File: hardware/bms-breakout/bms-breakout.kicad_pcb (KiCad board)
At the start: 2 copper layers, 115.6 x 85.8 mm, 14 parts, among them J1 IN-A, J10 V-SUPP, J11 Smol_Brain_Board, J12 DE9_Socket_MountingHoles, J13 UART_CONN, J15 SBB_POWER, J2 IN-B, J3 IN-C, J4 BALANCE-A, J5 BALANCE-B, J6 BALANCE-C, J8 BMS-OUT, J9 BMS-IN

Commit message: WIP: Starting firmware and routing pcb
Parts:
- moved J15 79.1 mm to (148.2, 124.0), turned to 180 degrees
- moved J9 10.1 mm to (174.9, 112.6)
- moved J10 9.91 mm to (155.3, 91.5)
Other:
- board size 115.6 x 85.8 mm -> 125.8 x 85.8 mm
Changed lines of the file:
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@@
 	(version 20241229)
 	(generator "pcbnew")
-	(generator_version "9.0")
+	(generator_version "9.99")
 	(general
 		(thickness 1.6)
@@
 	(footprint "Connector_AMASS:AMASS_XT90PW-M_1x02_P10.90mm_Horizontal"
 		(layer "F.Cu")
-		(at 164.85 112.05 180)
+		(at 174.9 112.6 180)
 		(descr "Connector XT90 Horizontal PCB Male  500V 30A IP40, https://www.bto.pl/pdf/09025/XT90PW-M.pdf")
 		(tags "RC")
@@
 	(footprint "Connector_AMASS:AMASS_XT30PW-M_1x02_P2.50mm_Horizontal"
 		(layer "F.Cu")
-		(at 69.575 115.2 90)
+		(at 148.2 124 180)
 		(descr "Connector XT30 Horizontal PCB Male, https://www.tme.eu/Document/6eb2005a51a52592b3f19e8a450c54c8/XT30PW-M.pdf")
 		(tags "RC Connector XT30")
 		(property "Reference" "J15"
-			(at 2.4 -2.675 90)
+			(at 2.4 -2.675 0)
 			(layer "F.SilkS")
 			(effects
@@
 		)
 		(property "Value" "SBB_POWER"
-			(at -2.5 3.5 90)
+			(at -2.5 3.5 0)
 			(layer "F.Fab")
 			(effects
@@
 		)
 		(property "Datasheet" "~"
-			(at 0 0 90)
+			(at 0 0 180)
 			(unlocked yes)
 			(layer "F.Fab")
@@
 		)
 		(property "Description" "Generic connectable mounting pin connector, single row, 01x02, script generated (kicad-library-utils/schlib/autogen/connector/)"
-			(at 0 0 90)
+			(at 0 0 180)
 			(unlocked yes)
 			(layer "F.Fab")
@@
 		(attr through_hole)
 		(fp_line
-			(start 2.56 -13.21)
-			(end 2.56 -11.11)
+			(start 2.56 -8.89)
+			(end 3.15 -8.89)
 			(stroke
 				(width 0.12)
@@
 		)
 		(fp_line
-			(start -7.56 -13.21)
-			(end 2.56 -13.21)
+			(start 2.56 -8.89)
+			(end 2.56 -3.99)
 			(stroke
 				(width 0.12)
@@
 		)
 		(fp_line
-			(start -7.56 -13.21)
-			(end -7.56 -11.11)
+			(start 2.56 -11.11)
+			(end 3.15 -11.11)
 			(stroke
 				(width 0.12)
@@
 		)
 		(fp_line
-			(start 2.56 -11.11)
-			(end 3.15 -11.11)
+			(start 2.56 -13.21)
+			(end 2.56 -11.11)
 			(stroke
 				(width 0.12)
@@
 		)
 		(fp_line
-			(start -8.15 -11.11)
-			(end -7.56 -11.11)
+			(start -7.56 -3.99)
+			(end 2.56 -3.99)
 			(stroke
 				(width 0.12)
@@
 		)
 		(fp_line
-			(start 2.56 -8.89)
-			(end 3.15 -8.89)
+			(start -7.56 -8.89)
+			(end -7.56 -3.99)
 			(stroke
 				(width 0.12)
@@
 		)
 		(fp_line
-			(start 2.56 -8.89)
-			(end 2.56 -3.99)
+			(start -7.56 -13.21)
+			(end 2.56 -13.21)
 			(stroke
 				(width 0.12)
@@
 		)
 		(fp_line
-			(start -7.56 -8.89)
-			(end -7.56 -3.99)
+			(start -7.56 -13.21)
+			(end -7.56 -11.11)
 			(stroke
 				(width 0.12)
@@
 		)
 		(fp_line
-			(start -7.56 -3.99)
-			(end 2.56 -3.99)
+			(start -8.15 -11.11)
+			(end -7.56 -11.11)
 			(stroke
 				(width 0.12)
@@
 		)
 		(fp_line
-			(start -9.65 -13.6)
-			(end 4.65 -13.6)
+			(start -9.65 2.25)
+			(end 4.65 2.25)
 			(stroke
 				(width 0.05)
@@
 		(fp_line
 			(start -9.65 -13.6)
-			(end -9.65 2.25)
+			(end 4.65 -13.6)
 			(stroke
 				(width 0.05)
@@
 		)
 		(fp_line
-			(start -9.65 2.25)
-			(end 4.65 2.25)
+			(start -9.65 -13.6)
+			(end -9.65 2.25)
 			(stroke
 				(width 0.05)
@@
 		)
 		(fp_line
-			(start 2.45 -13.1)
-			(end 2.45 -11)
+			(start 2.45 -9)
+			(end 3.15 -9)
 			(stroke
 				(width 0.1)
@@
 		)
 		(fp_line
-			(start -7.45 -13.1)
-			(end 2.45 -13.1)
+			(start 2.45 -9)
+			(end 2.45 -4.1)
 			(stroke
 				(width 0.1)
@@
 		)
 		(fp_line
-			(start -7.45 -13.1)
-			(end -7.45 -11)
+			(start 2.45 -11)
+			(end 3.15 -11)
 			(stroke
 				(width 0.1)
@@
 		)
 		(fp_line
-			(start 2.45 -11)
-			(end 3.15 -11)
+			(start 2.45 -13.1)
+			(end 2.45 -11)
 			(stroke
 				(width 0.1)
@@
 		)
 		(fp_line
-			(start -8.15 -11)
-			(end -7.45 -11)
+			(start -7.45 -4.1)
+			(end 2.45 -4.1)
 			(stroke
 				(width 0.1)
@@
 		)
 		(fp_line
-			(start 2.45 -9)
-			(end 3.15 -9)
+			(start -7.45 -9)
+			(end -7.45 -4.1)
 			(stroke
 				(width 0.1)
@@
 		)
 		(fp_line
-			(start 2.45 -9)
-			(end 2.45 -4.1)
+			(start -7.45 -13.1)
+			(end 2.45 -13.1)
 			(stroke
 				(width 0.1)
@@
 		)
 		(fp_line
-			(start -7.45 -9)
-			(end -7.45 -4.1)
+			(start -7.45 -13.1)
+			(end -7.45 -11)
 			(stroke
 				(width 0.1)
@@
 		)
 		(fp_line
-			(start -7.45 -4.1)
-			(end 2.45 -4.1)
+			(start -8.15 -11)
+			(end -7.45 -11)
 			(stroke
 				(width 0.1)
@@
 		)
 		(fp_text user "-"
-			(at 3 0 90)
+			(at 3 0 0)
 			(layer "F.SilkS")
 			(effects
@@
 		)
 		(fp_text user "+"
-			(at -8 0 90)
+			(at -8 0 0)
 			(layer "F.SilkS")
 			(effects
@@
 		)
 		(fp_text user "${REFERENCE}"
-			(at -2.5 -3 90)
+			(at -2.5 -3 0)
 			(layer "F.Fab")
 			(effects
@@
 		)
 		(pad "" thru_hole circle
-			(at -8 -10 90)
+			(at -8 -10 180)
 			(size 1.4 1.4)
 			(drill 1)
@@
 		)
 		(pad "" thru_hole circle
-			(at 3 -10 90)
+			(at 3 -10 180)
 			(size 1.4 1.4)
 			(drill 1)
@@
 		)
 		(pad "1" thru_hole roundrect
-			(at 0 0 90)
+			(at 0 0 180)
 			(size 3.5 3.5)
 			(drill 1.9)
@@
 		)
 		(pad "2" thru_hole circle
-			(at -5 0 90)
+			(at -5 0 180)
 			(size 3.5 3.5)
 			(drill 1.9)
@@
 	(footprint "Connector_AMASS:AMASS_XT90PW-M_1x02_P10.90mm_Horizontal"
 		(layer "F.Cu")
-		(at 145.4 91.1 -90)
+		(at 155.3 91.55 -90)
 		(descr "Connector XT90 Horizontal PCB Male  500V 30A IP40, https://www.bto.pl/pdf/09025/XT90PW-M.pdf")
 		(tags "RC")
@@
 	(gr_rect
 		(start 55.5 52.4)
-		(end 171.1 138.2)
+		(end 181.3 138.2)
 		(stroke
 			(width 0.05)

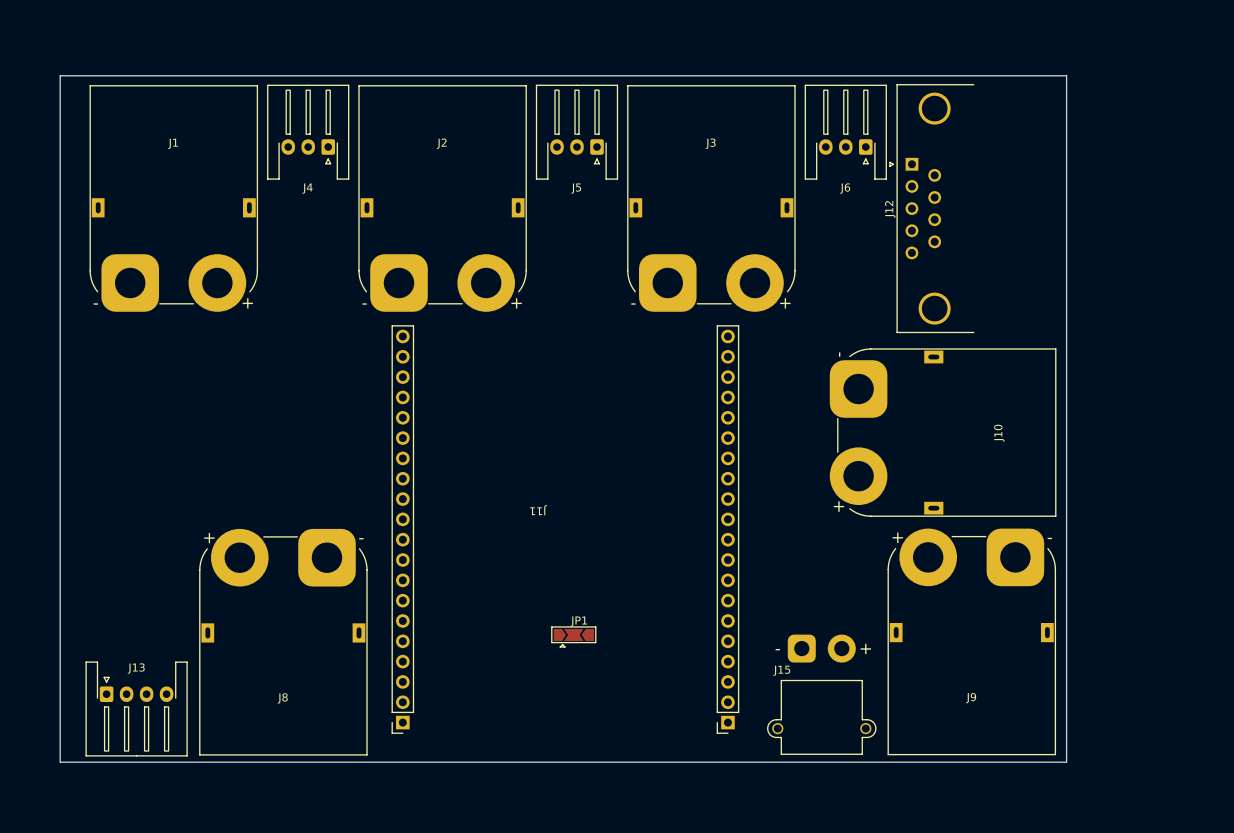
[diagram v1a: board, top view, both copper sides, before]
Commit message: Started Traces
- Finished first draft of schematic
- Started first draft of traces
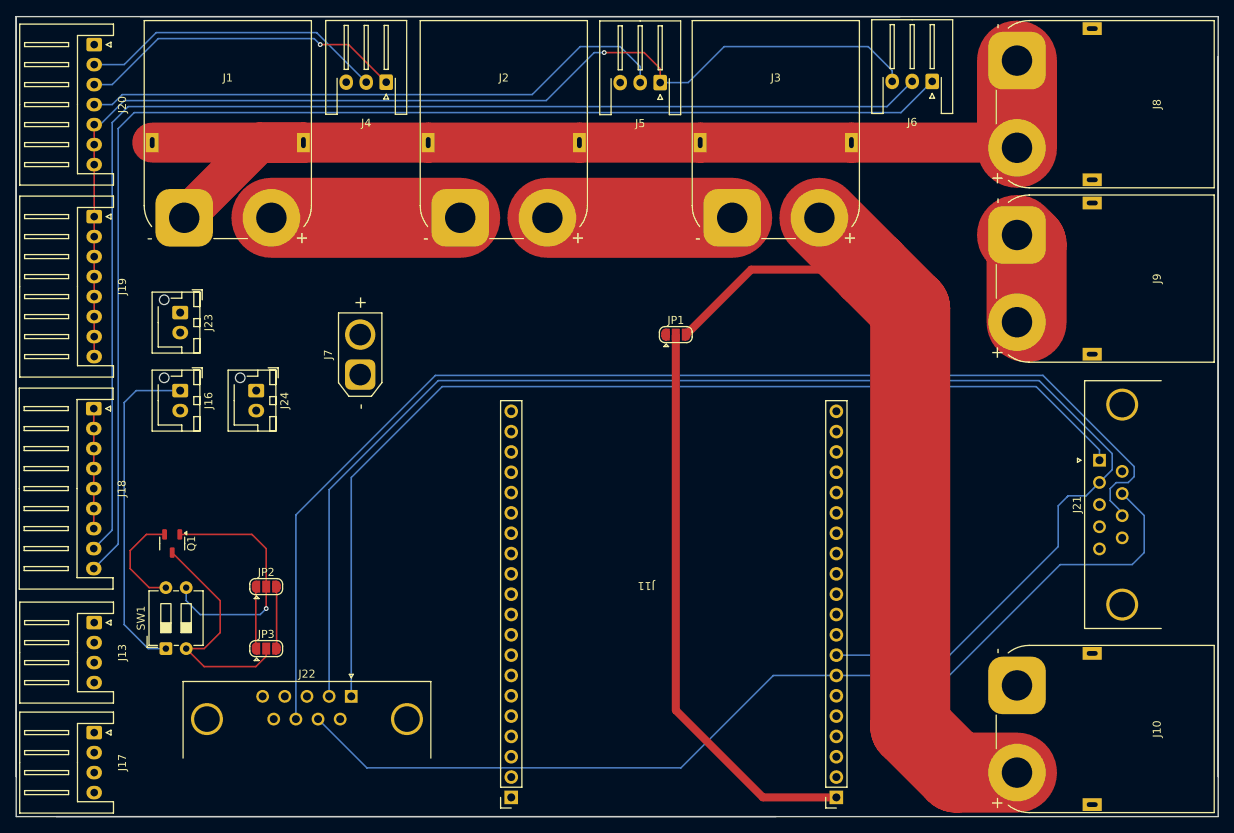
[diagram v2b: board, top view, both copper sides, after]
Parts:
- removed J12: DE9_Socket_MountingHoles, Connector_Dsub:DSUB-9_Socket_Horizontal_P2.77x2.84mm_EdgePinOffset4.94mm_Housed_MountingHolesOffset4.94mm
- removed J15: SBB_POWER, Connector_AMASS:AMASS_XT30PW-M_1x02_P2.50mm_Horizontal
- added J16: ESTOP_CON, Connector_JST:JST_XH_B2B-XH-AM_1x02_P2.50mm_Vertical, F.Cu at (70.5, 91.8)
- added J17: I2C_Conn, Connector_JST:JST_XH_S4B-XH-A_1x04_P2.50mm_Horizontal, F.Cu at (59.8, 134.5)
- added J18: BAL_3, Connector_JST:JST_XH_S9B-XH-A_1x09_P2.50mm_Horizontal, F.Cu at (59.7, 94.0)
- added J19: BAL_2, Connector_JST:JST_XH_S8B-XH-A_1x08_P2.50mm_Horizontal, F.Cu at (59.8, 70.0)
- added J20: BAL_1, Connector_JST:JST_XH_S7B-XH-A_1x07_P2.50mm_Horizontal, F.Cu at (59.8, 48.5)
- added J21: DE9_Socket_MountingHoles, Connector_Dsub:DSUB-9_Socket_Horizontal_P2.77x2.84mm_EdgePinOffset4.94mm_Housed_MountingHolesOffset4.94mm, F.Cu at (185.4, 100.5)
- added J22: DE9_Socket_MountingHoles, Connector_Dsub:DSUB-9_Socket_Horizontal_P2.77x2.84mm_EdgePinOffset4.94mm_Housed_MountingHolesOffset4.94mm, F.Cu at (91.9, 130.0)
- added J23: FAN-IN, Connector_JST:JST_XH_B2B-XH-AM_1x02_P2.50mm_Vertical, F.Cu at (70.5, 82.0)
- added J24: SWITCH, Connector_JST:JST_XH_B2B-XH-AM_1x02_P2.50mm_Vertical, F.Cu at (80.0, 91.8)
- added J7: Conn_01x02, Connector_AMASS:AMASS_XT30U-M_1x02_P5.0mm_Vertical, F.Cu at (93.0, 89.8)
- added JP2: Drain_Side, Jumper:SolderJumper-3_P1.3mm_Open_RoundedPad1.0x1.5mm, F.Cu at (81.2, 116.2)
- added JP3: Source_Side, Jumper:SolderJumper-3_P1.3mm_Open_RoundedPad1.0x1.5mm, F.Cu at (81.2, 124.0)
- added Q1: PMOZZ, Package_TO_SOT_SMD:SOT-23-3, F.Cu at (69.5, 110.9)
- added SW1: SW_DIP_x02, Button_Switch_THT:SW_DIP_SPSTx02_Slide_6.7x6.64mm_W7.62mm_P2.54mm_LowProfile, F.Cu at (68.7, 124.0)
- J13: footprint Connector_JST:JST_XH_S4B-XH-A-1_1x04_P2.50mm_Horizontal -> Connector_JST:JST_XH_S4B-XH-A_1x04_P2.50mm_Horizontal
- JP1: value SolderJumper_3_Open -> VCC-VBUS; footprint Jumper:SolderJumper-3_P2.0mm_Open_TrianglePad1.0x1.5mm -> Jumper:SolderJumper-3_P1.3mm_Open_RoundedPad1.0x1.5mm
- moved J8 106.3 mm to (175.1, 50.5), turned to -90 degrees
- moved J10 42.0 mm to (175.1, 128.6)
- moved J9 40.3 mm to (175.1, 72.3), turned to -90 degrees
- moved JP1 39.7 mm to (132.4, 84.8)
- moved J11 16.5 mm to (128.8, 115.7)
- moved J6 11.7 mm to (164.5, 53.1)
- moved J3 11.5 mm to (139.5, 70.2)
- moved J5 11.3 mm to (130.5, 53.2)
- moved J2 11.2 mm to (105.5, 70.2)
- moved J4 10.9 mm to (96.2, 53.2)
- moved J1 10.6 mm to (71.0, 70.2)
- moved J13 9.08 mm to (59.8, 120.8), turned to -90 degrees
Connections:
- net GND2 renamed GND_C
- J1 pad 1: GND1 -> GND_B
- J1 pad MP: GND1 -> GND_B
- J11 pad 22: /SW -> unconnected-(J11-IO13-Pad22)
- J11 pad 3: /UART_TX -> unconnected-(J11-UART0_TX-Pad3)
- J11 pad 38: unconnected-(J11-I2C_SDA-Pad38) -> /I2C_SDA
- J11 pad 39: unconnected-(J11-I2C_SCK-Pad39) -> /I2C_SCK
- J11 pad 4: /UART_RX -> unconnected-(J11-UART0_RX-Pad4)
- J11 pad 5: unconnected-(J11-UART1_TX-Pad5) -> /UART_TX
- J11 pad 6: unconnected-(J11-UART1_RX-Pad6) -> /UART_RX
- J11 pad 7: /CAN_H -> /CAN_H_A
- J11 pad 8: /CAN_L -> /CAN_L_A
- J2 pad MP: GND1 -> GND_B
- J3 pad MP: GND1 -> GND_B
- J4 pad 3: /BAL_0 -> GND_B
- J8 pad 1: GND1 -> GND_B
- J8 pad 2: GND1 -> GND_B
- J8 pad MP: GND1 -> GND_B
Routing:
- net /CAN_L_A: track 0.00 -> 182.4 mm
- net /BAL_6: track 0.00 -> 160.5 mm
- net /BAL_5: track 0.00 -> 156.3 mm
- net /BAL_4: track 0.00 -> 154.5 mm, vias 0 -> 1
- net /CAN_H_B: track 0.00 -> 151.1 mm
- net GND_B: track 0.00 -> 138.1 mm
- net /CAN_L_B: track 0.00 -> 130.2 mm
- net /CAN_H_A: track 0.00 -> 125.5 mm
- net VBUS: track 0.00 -> 110.5 mm
- net /BAL_3: track 0.00 -> 74.3 mm
- net Net-(J11-VCC): track 0.00 -> 71.5 mm
- net Net-(J16-Pin_1): track 0.00 -> 41.8 mm
- net /BAL_2: track 0.00 -> 41.1 mm, vias 0 -> 1
- net /BAL_1: track 0.00 -> 38.2 mm
- net Net-(JP2-C): track 0.00 -> 31.7 mm, vias 0 -> 1
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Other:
- board size 125.8 x 85.8 mm -> 150.2 x 100 mm
